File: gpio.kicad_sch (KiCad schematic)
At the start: 19 parts, among them J10 GPIO0, J13 GPIO1, J16 SCOOP1, J17 SCOOP2, J18 ACTUATOR, J19 DRILL, J20 SERVO5, J21 SERVO6, J22 SERVO7, J23 SERVO8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

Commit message: more cleanup and added notes for review
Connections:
- net Payload_S1: now also J10.1 (Pin_1), U8.4 (IO0_0); no longer J10.5 (Pin_5), U8.8 (IO0_4)
- net Payload_S2: now also J10.2 (Pin_2), U8.5 (IO0_1); no longer J10.6 (Pin_6), U8.9 (IO0_5)
- net Payload_S3: now also J10.3 (Pin_3), U8.6 (IO0_2); no longer J10.7 (Pin_7), U8.10 (IO0_6)
- net Payload_S4: now also J10.4 (Pin_4), U8.7 (IO0_3); no longer J10.8 (Pin_8), U8.11 (IO0_7)
- net GP21 renamed DIGITAL_GP21
- net GP22 renamed DIGITAL_GP22
- net NEW_GP14 renamed DIGITAL_GP14
- net NEW_GP15 renamed DIGITAL_GP15
- new net: J10.7 (Pin_7), U8.10 (IO0_6)
- new net: J10.8 (Pin_8), U8.11 (IO0_7)
- new net: J10.5 (Pin_5), U8.8 (IO0_4)
- new net: J10.6 (Pin_6), U8.9 (IO0_5)
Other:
- note added: "------ GET RID? -----"
- note added: "POSSIBILITIES!"
- note added: "WHAT DOES THE MANIPULATOR USE LABEL THE RELAYS FERRITES AND ESD?"

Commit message: DNP unused connectors for now
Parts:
- J10, J13, J20, J21, J22, J23: now not fitted
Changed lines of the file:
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@@
 		(in_bom yes)
 		(on_board yes)
-		(dnp no)
+		(dnp yes)
 		(fields_autoplaced yes)
 		(property "Reference" "J22"
@@
 		(in_bom yes)
 		(on_board yes)
-		(dnp no)
+		(dnp yes)
 		(fields_autoplaced yes)
 		(property "Reference" "J21"
@@
 		(in_bom yes)
 		(on_board yes)
-		(dnp no)
+		(dnp yes)
 		(fields_autoplaced yes)
 		(property "Reference" "J20"
@@
 		(in_bom yes)
 		(on_board yes)
-		(dnp no)
+		(dnp yes)
 		(fields_autoplaced yes)
 		(property "Reference" "J10"
@@
 		(in_bom yes)
 		(on_board yes)
-		(dnp no)
+		(dnp yes)
 		(fields_autoplaced yes)
 		(property "Reference" "J13"
@@
 		(in_bom yes)
 		(on_board yes)
-		(dnp no)
+		(dnp yes)
 		(fields_autoplaced yes)
 		(property "Reference" "J23"

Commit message: pcb review session notes
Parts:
- J9: value RELAYS -> GPIO
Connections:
- net DIGITAL_GP15 is gone; now on net DIGITAL_LIMIT_SW: J9.6 (Pin_6)
- net DIGITAL_GP14 renamed DIGITAL_LIMIT_SW
- net DIGITAL_GP21 renamed DIGITAL_RELAY1
- net DIGITAL_GP22 renamed DIGITAL_RELAY2
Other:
- note added: "LIMIT SWITCHES I2C to USB converter"
- moved on the sheet: J10, J13
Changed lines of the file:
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@@
 		)
 	)
+	(text "LIMIT SWITCHES\nI2C to USB converter"
+		(exclude_from_sim no)
+		(at 121.158 103.632 0)
+		(effects
+			(font
+				(size 2.54 2.54)
+				(thickness 0.508)
+				(bold yes)
+				(color 255 0 0 1)
+			)
+			(justify left top)
+		)
+	)
 	(text "3 and 4 go to the big\nconnector on Daedalus."
 		(exclude_from_sim no)
@@
 	(text "------ GET RID? -----\n"
 		(exclude_from_sim no)
-		(at 240.538 152.146 90)
+		(at 244.094 156.21 90)
 		(effects
 			(font
@@
 	(text "POSSIBILITIES!"
 		(exclude_from_sim no)
-		(at 46.482 150.622 0)
+		(at 33.274 150.114 0)
 		(effects
 			(font
@@
 	(wire
 		(pts
-			(xy 93.98 133.35) (xy 113.03 133.35)
+			(xy 93.98 133.35) (xy 114.3 133.35)
 		)
 		(stroke
@@
 	(wire
 		(pts
-			(xy 93.98 135.89) (xy 113.03 135.89)
+			(xy 93.98 135.89) (xy 114.3 135.89)
 		)
 		(stroke
@@
 	(wire
 		(pts
-			(xy 113.03 163.83) (xy 93.98 163.83)
+			(xy 114.3 163.83) (xy 93.98 163.83)
 		)
 		(stroke
@@
 	(wire
 		(pts
-			(xy 93.98 171.45) (xy 113.03 171.45)
+			(xy 93.98 171.45) (xy 114.3 171.45)
 		)
 		(stroke
@@
 	(wire
 		(pts
-			(xy 93.98 168.91) (xy 113.03 168.91)
+			(xy 93.98 168.91) (xy 114.3 168.91)
 		)
 		(stroke
@@
 	(wire
 		(pts
-			(xy 93.98 138.43) (xy 113.03 138.43)
+			(xy 93.98 138.43) (xy 114.3 138.43)
 		)
 		(stroke
@@
 	(wire
 		(pts
-			(xy 93.98 148.59) (xy 113.03 148.59)
+			(xy 93.98 148.59) (xy 114.3 148.59)
 		)
 		(stroke
@@
 	(wire
 		(pts
-			(xy 93.98 161.29) (xy 113.03 161.29)
+			(xy 93.98 161.29) (xy 114.3 161.29)
 		)
 		(stroke
@@
 	(wire
 		(pts
-			(xy 113.03 153.67) (xy 93.98 153.67)
+			(xy 114.3 153.67) (xy 93.98 153.67)
 		)
 		(stroke
@@
 	(wire
 		(pts
-			(xy 93.98 140.97) (xy 113.03 140.97)
+			(xy 93.98 140.97) (xy 114.3 140.97)
 		)
 		(stroke
@@
 	(wire
 		(pts
-			(xy 93.98 156.21) (xy 113.03 156.21)
+			(xy 93.98 156.21) (xy 114.3 156.21)
 		)
 		(stroke
@@
 	(wire
 		(pts
-			(xy 113.03 158.75) (xy 93.98 158.75)
+			(xy 114.3 158.75) (xy 93.98 158.75)
 		)
 		(stroke
@@
 	(wire
 		(pts
-			(xy 93.98 143.51) (xy 113.03 143.51)
+			(xy 93.98 143.51) (xy 114.3 143.51)
 		)
 		(stroke
@@
 	(wire
 		(pts
-			(xy 93.98 130.81) (xy 113.03 130.81)
+			(xy 93.98 130.81) (xy 114.3 130.81)
 		)
 		(stroke
@@
 	(wire
 		(pts
-			(xy 113.03 166.37) (xy 93.98 166.37)
+			(xy 114.3 166.37) (xy 93.98 166.37)
 		)
 		(stroke
@@
 	(wire
 		(pts
-			(xy 93.98 146.05) (xy 113.03 146.05)
+			(xy 93.98 146.05) (xy 114.3 146.05)
 		)
 		(stroke
@@
 		)
 	)
-	(global_label "DIGITAL_GP22"
+	(global_label "DIGITAL_RELAY2"
 		(shape input)
 		(at 115.57 57.15 180)
@@
 		)
 		(property "Intersheetrefs" "${INTERSHEET_REFS}"
-			(at 100.4785 57.15 0)
+			(at 98.6037 57.15 0)
 			(effects
 				(font
@@
 		)
 	)
-	(global_label "DIGITAL_GP15"
+	(global_label "DIGITAL_LIMIT_SW"
 		(shape input)
 		(at 115.57 62.23 180)
@@
 		)
 		(property "Intersheetrefs" "${INTERSHEET_REFS}"
-			(at 100.4785 62.23 0)
+			(at 97.1523 62.23 0)
 			(effects
 				(font
@@
 		)
 	)
-	(global_label "DIGITAL_GP14"
+	(global_label "DIGITAL_LIMIT_SW"
 		(shape input)
 		(at 115.57 59.69 180)
@@
 		)
 		(property "Intersheetrefs" "${INTERSHEET_REFS}"
-			(at 100.4785 59.69 0)
+			(at 97.1523 59.69 0)
 			(effects
 				(font
@@
 		)
 	)
-	(global_label "DIGITAL_GP21"
+	(global_label "DIGITAL_RELAY1"
 		(shape input)
 		(at 115.57 54.61 180)
@@
 		)
 		(property "Intersheetrefs" "${INTERSHEET_REFS}"
-			(at 100.4785 54.61 0)
+			(at 98.6037 54.61 0)
 			(effects
 				(font
@@
 	(symbol
 		(lib_id "Connector_Generic:Conn_01x08")
-		(at 118.11 138.43 0)
+		(at 119.38 138.43 0)
 		(unit 1)
 		(exclude_from_sim no)
@@
 		(fields_autoplaced yes)
 		(property "Reference" "J10"
-			(at 120.65 138.4299 0)
+			(at 121.92 138.4299 0)
 			(effects
 				(font
@@
 		)
 		(property "Value" "GPIO0"
-			(at 120.65 140.9699 0)
+			(at 121.92 140.9699 0)
 			(effects
 				(font
@@
 		)
 		(property "Footprint" "Connector_Molex:Molex_PicoBlade_53047-0810_1x08_P1.25mm_Vertical"
-			(at 118.11 138.43 0)
+			(at 119.38 138.43 0)
 			(effects
 				(font
@@
 		)
 		(property "Datasheet" "~"
-			(at 118.11 138.43 0)
+			(at 119.38 138.43 0)
 			(effects
 				(font
@@
 		)
 		(property "Description" "Generic connector, single row, 01x08, script generated (kicad-library-utils/schlib/autogen/connector/)"
-			(at 118.11 138.43 0)
+			(at 119.38 138.43 0)
 			(effects
 				(font
@@
 		)
 		(property "Manufacturer" ""
-			(at 118.11 138.43 0)
+			(at 119.38 138.43 0)
 			(effects
 				(font
@@
 		)
 		(property "Manufacturer Part Number" ""
-			(at 118.11 138.43 0)
+			(at 119.38 138.43 0)
 			(effects
 				(font
@@
 		)
 		(property "Vendor" ""
-			(at 118.11 138.43 0)
+			(at 119.38 138.43 0)
 			(effects
 				(font
@@
 		)
 		(property "Vendor Part Number" ""
-			(at 118.11 138.43 0)
+			(at 119.38 138.43 0)
 			(effects
 				(font
@@
 		)
 		(property "Comments" ""
-			(at 118.11 138.43 0)
+			(at 119.38 138.43 0)
 			(effects
 				(font
@@
 		)
 		(property "Notes" ""
-			(at 118.11 138.43 0)
+			(at 119.38 138.43 0)
 			(effects
 				(font
@@
 	(symbol
 		(lib_id "Connector_Generic:Conn_01x08")
-		(at 118.11 161.29 0)
+		(at 119.38 161.29 0)
 		(unit 1)
 		(exclude_from_sim no)
@@
 		(fields_autoplaced yes)
 		(property "Reference" "J13"
-			(at 120.65 161.2899 0)
+			(at 121.92 161.2899 0)
 			(effects
 				(font
@@
 		)
 		(property "Value" "GPIO1"
-			(at 120.65 163.8299 0)
+			(at 121.92 163.8299 0)
 			(effects
 				(font
@@
 		)
 		(property "Footprint" "Connector_Molex:Molex_PicoBlade_53047-0810_1x08_P1.25mm_Vertical"
-			(at 118.11 161.29 0)
+			(at 119.38 161.29 0)
 			(effects
 				(font
@@
 		)
 		(property "Datasheet" "~"
-			(at 118.11 161.29 0)
+			(at 119.38 161.29 0)
 			(effects
 				(font
@@
 		)
 		(property "Description" "Generic connector, single row, 01x08, script generated (kicad-library-utils/schlib/autogen/connector/)"
-			(at 118.11 161.29 0)
+			(at 119.38 161.29 0)
 			(effects
 				(font
@@
 		)
 		(property "Manufacturer" ""
-			(at 118.11 161.29 0)
+			(at 119.38 161.29 0)
 			(effects
 				(font
@@
 		)
 		(property "Manufacturer Part Number" ""
-			(at 118.11 161.29 0)
+			(at 119.38 161.29 0)
 			(effects
 				(font
@@
 		)
 		(property "Vendor" ""
-			(at 118.11 161.29 0)
+			(at 119.38 161.29 0)
 			(effects
 				(font
@@
 		)
 		(property "Vendor Part Number" ""
-			(at 118.11 161.29 0)
+			(at 119.38 161.29 0)
 			(effects
 				(font
@@
 		)
 		(property "Comments" ""
-			(at 118.11 161.29 0)
+			(at 119.38 161.29 0)
 			(effects
 				(font
@@
 		)
 		(property "Notes" ""
-			(at 118.11 161.29 0)
+			(at 119.38 161.29 0)
 			(effects
 				(font
@@
 			)
 		)
-		(property "Value" "RELAYS"
+		(property "Value" "GPIO"
 			(at 135.89 59.6899 0)
 			(effects

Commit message: major rework again after the meeting
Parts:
- removed J10: GPIO0, Connector_Molex:Molex_PicoBlade_53047-0810_1x08_P1.25mm_Vertical, symbol Connector_Generic:Conn_01x08
- removed J13: GPIO1, Connector_Molex:Molex_PicoBlade_53047-0810_1x08_P1.25mm_Vertical, symbol Connector_Generic:Conn_01x08
- removed J20: SERVO5, Connector_Molex:Molex_PicoBlade_53047-0310_1x03_P1.25mm_Vertical, symbol Connector_Generic:Conn_01x03
- removed J21: SERVO6, Connector_Molex:Molex_PicoBlade_53047-0310_1x03_P1.25mm_Vertical, symbol Connector_Generic:Conn_01x03
- removed J22: SERVO7, Connector_Molex:Molex_PicoBlade_53047-0310_1x03_P1.25mm_Vertical, symbol Connector_Generic:Conn_01x03
- removed J23: SERVO8, Connector_Molex:Molex_PicoBlade_53047-0310_1x03_P1.25mm_Vertical, symbol Connector_Generic:Conn_01x03
- removed R7: 10k, Resistor_SMD:R_0805_2012Metric_Pad1.20x1.40mm_HandSolder, symbol Device:R_US
- removed U15: 74HCT244, Package_SO:SO-20_12.8x7.5mm_P1.27mm, symbol 74xx:74HCT244
- removed U8: PCA9555PWR, Package_SO:TSSOP-24_4.4x7.8mm_P0.65mm, symbol Interface_Expansion:PCA9555DB
- added U1: SN74AHCT126DR, Package_SO:SOIC-14_3.9x8.7mm_P1.27mm, symbol symbols:SN74AHCT126DR
- J16: value SCOOP1 -> SCOOP
- J17: value SCOOP2 -> MANIPULATOR
- J18: value ACTUATOR -> SERVO3
- J19: value DRILL -> SERVO4
- J7: value POT3 -> MANIPULATOR
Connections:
- net VDC is gone; now on net +5V: C25.1, J16.1 (Pin_1), J17.1 (Pin_1), J18.1 (Pin_1), J19.1 (Pin_1)
- net +5V: now also U1.1 (1OE), U1.10 (3OE), U1.13 (4OE), U1.14 (VCC), U1.4 (2OE)
- net GND: now also U1.7 (GND)
- net SERVO1_OUT: now also U1.3 (1Y)
- net SERVO1_PICO: now also U1.2 (1A)
- net SERVO2_OUT: now also U1.6 (2Y)
- net SERVO2_PICO: now also U1.5 (2A)
- net SERVO3_OUT: now also U1.8 (3Y)
- net SERVO3_PICO: now also U1.9 (3A)
- net SERVO4_OUT: now also U1.11 (4Y)
- net SERVO4_PICO: now also U1.12 (4A)
- net ANALOG_POT3 renamed ANALOG_MANIPULATOR
- net DIGITAL_LIMIT_SW renamed DIGITAL_LIMIT_SW1
- net DIGITAL_LIMIT_SW1: no longer J9.6 (Pin_6)
- new net DIGITAL_LIMIT_SW2: J9.6 (Pin_6)
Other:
- note removed: "------ GET RID? -----"
- note removed: "Address: 0x20"
- note removed: "GPIO EXPANSION"
- note removed: "LIMIT SWITCHES I2C to USB converter"
- note removed: "NOTE: can use PCA9555 or TCA9555"
- note removed: "POSSIBILITIES!"
- note removed: "WHAT DOES THE MANIPULATOR USE LABEL THE RELAYS FERRITES AND ESD?"
- moved on the sheet: C23, C25, J16, J17, J18, J19, J5, J6, J7, J9

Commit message: major finishing touches:     - major rework for v5.1     - silkscreen and stuff     - impednace for USB and CAN lines     - schematic comments     - symbol, footprint, and model library updates
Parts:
- added C10: 1000uF, Capacitor_THT:CP_Radial_D10.0mm_P5.00mm, symbol Device:C_Polarized_US
- added J10: QWIIC3, Connector_JST:JST_GH_BM04B-GHS-TBT_1x04-1MP_P1.25mm_Vertical, symbol Connector_Generic:Conn_01x04
- added J11: QWIIC2, Connector_JST:JST_GH_BM04B-GHS-TBT_1x04-1MP_P1.25mm_Vertical, symbol Connector_Generic:Conn_01x04
- added J13: QWIIC1, Connector_JST:JST_GH_BM04B-GHS-TBT_1x04-1MP_P1.25mm_Vertical, symbol Connector_Generic:Conn_01x04
- added J20: EXP1, Connector_PinSocket_2.54mm:PinSocket_1x06_P2.54mm_Vertical, symbol Connector_Generic:Conn_01x06
- added J21: EXP2, Connector_PinSocket_2.54mm:PinSocket_1x06_P2.54mm_Vertical, symbol Connector_Generic:Conn_01x06
- added J22: EXP3, Connector_PinSocket_2.54mm:PinSocket_1x06_P2.54mm_Vertical, symbol Connector_Generic:Conn_01x06
- added J23: EXP4, Connector_PinSocket_2.54mm:PinSocket_1x06_P2.54mm_Vertical, symbol Connector_Generic:Conn_01x06
- added J8: QWIIC4, Connector_JST:JST_GH_BM04B-GHS-TBT_1x04-1MP_P1.25mm_Vertical, symbol Connector_Generic:Conn_01x04
- added R11, R12, R13, R14, R15, R16: 10k, Resistor_SMD:R_0603_1608Metric_Pad0.98x0.95mm_HandSolder, symbol Device:R_US
- added SW1: QUIIC, Button_Switch_THT:SW_E-Switch_EG1271_SPDT, symbol Switch:SW_SPDT
- added SW2: EXP, Button_Switch_THT:SW_E-Switch_EG1271_SPDT, symbol Switch:SW_SPDT
- C23: value 0.1 uF -> 0.1uF; Manufacturer (none) -> KEMET; Manufacturer Part Number (none) -> C1206C104J5RACTU; Vendor (none) -> Digikey; Vendor Part Number (none) -> 399-C1206C104J5RACTUCT-ND
- C25: value 100 uF -> 1000uF; Manufacturer (none) -> Nichicon; Manufacturer Part Number (none) -> UVR1E102MPD; Vendor (none) -> Digikey; Vendor Part Number (none) -> 493-1065-ND
- J16: renamed from J19; Manufacturer (none) -> Molex; Manufacturer Part Number (none) -> 0530470310; Vendor (none) -> Digikey; Vendor Part Number (none) -> WM1732-ND
- J17: renamed from J18; Manufacturer (none) -> Molex; Manufacturer Part Number (none) -> 0530470310; Vendor (none) -> Digikey; Vendor Part Number (none) -> WM1732-ND
- J18: renamed from J17; Manufacturer (none) -> Molex; Manufacturer Part Number (none) -> 0530470310; Vendor (none) -> Digikey; Vendor Part Number (none) -> WM1732-ND
- J19: renamed from J16; Manufacturer (none) -> Molex; Manufacturer Part Number (none) -> 0530470310; Vendor (none) -> Digikey; Vendor Part Number (none) -> WM1732-ND
- J5: value MOIST -> MST; Manufacturer (none) -> Molex; Manufacturer Part Number (none) -> 0530470310; Vendor (none) -> Digikey; Vendor Part Number (none) -> WM1732-ND
- J6: value TEMP -> TMP; Manufacturer (none) -> Molex; Manufacturer Part Number (none) -> 0530470310; Vendor (none) -> Digikey; Vendor Part Number (none) -> WM1732-ND
- J7: value MANIPULATOR -> MPR; Manufacturer (none) -> Molex; Manufacturer Part Number (none) -> 0530470310; Vendor (none) -> Digikey; Vendor Part Number (none) -> WM1732-ND
- J9: value GPIO -> DIGITAL; Manufacturer (none) -> Molex; Manufacturer Part Number (none) -> 0530470810; Vendor (none) -> Digikey; Vendor Part Number (none) -> WM1737-ND
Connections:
- net +5V: now also J9.1 (Pin_1), SW1.3 (C), SW2.3 (C); no longer J9.2 (Pin_2)
- net DIGITAL_LIMIT_SW1: now also R11.1
- net DIGITAL_LIMIT_SW2: now also R12.1
- net GND: now also C10.2, J10.1 (Pin_1), J11.1 (Pin_1), J13.1 (Pin_1), J20.1 (Pin_1), J21.1 (Pin_1), J22.1 (Pin_1), J23.1 (Pin_1), J8.1 (Pin_1), R15.1, R16.1
- net +3.3V renamed +3V3
- net +3V3: now also J9.2 (Pin_2), R11.2, R12.2, SW1.1 (A), SW2.1 (A); no longer J9.1 (Pin_1)
- new net +EXP: C10.1, J20.2 (Pin_2), J21.2 (Pin_2), J22.2 (Pin_2), J23.2 (Pin_2), R13.2, R14.2, SW2.2 (B)
- new net +QUIIC: J10.2 (Pin_2), J11.2 (Pin_2), J13.2 (Pin_2), J8.2 (Pin_2), SW1.2 (B)
- new net DIGITAL_EXP1: J20.5 (Pin_5), J21.5 (Pin_5), J22.5 (Pin_5), J23.5 (Pin_5), R13.1, R16.2
- new net DIGITAL_EXP2: J20.6 (Pin_6), J21.6 (Pin_6), J22.6 (Pin_6), J23.6 (Pin_6), R14.1, R15.2
- new net I2C0_SCL: J10.4 (Pin_4), J11.4 (Pin_4), J13.4 (Pin_4), J20.4 (Pin_4), J21.4 (Pin_4), J22.4 (Pin_4), J23.4 (Pin_4), J8.4 (Pin_4)
- new net I2C0_SDA: J10.3 (Pin_3), J11.3 (Pin_3), J13.3 (Pin_3), J20.3 (Pin_3), J21.3 (Pin_3), J22.3 (Pin_3), J23.3 (Pin_3), J8.3 (Pin_3)
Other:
- note added: "CUSTOM EXPANSION MODULES"
- note added: "Optional room for custom modules developed in house for flexibility and future-proofing."
- note added: "STEMMA QT / QWIIC MODULES"
- note added: "Standardized 4-pin I2C connectors that allow easy, solder-free chaining of off-the-shelf sensors and peripherals."
- company: WVU Unviersity Rover Challenge -> WVU Unviersity Rover Challenge (URC)
- moved on the sheet: C23, C25, J16, J17, J18, J19, J5, J6, J7, J9, U1

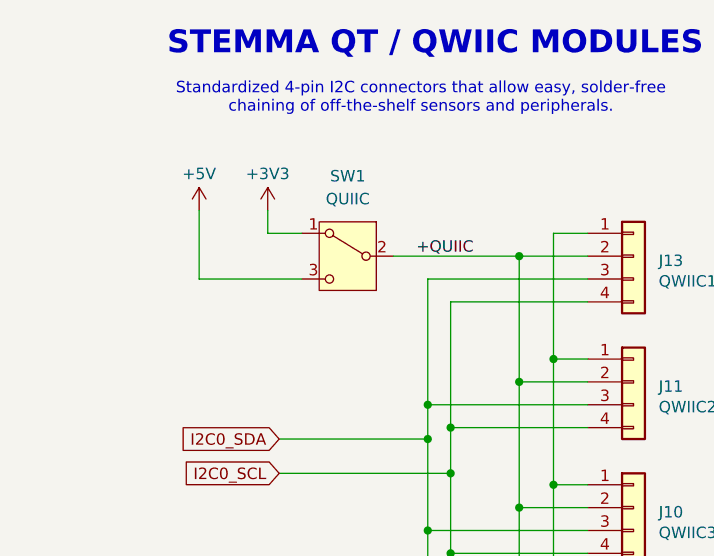
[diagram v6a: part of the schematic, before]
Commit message: swapped UART to USB from FTDI (out of stock) to MCP2200
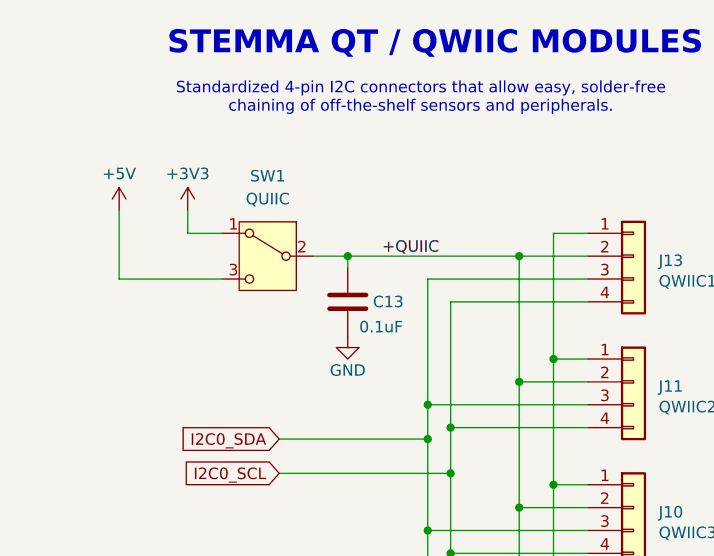
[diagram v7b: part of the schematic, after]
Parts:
- added C13: 0.1uF, Capacitor_SMD:C_1206_3216Metric_Pad1.33x1.80mm_HandSolder, symbol Device:C
- J10, J11, J13, J8: Manufacturer Part Number 455-1566-1-ND -> SM04B-GHS-TB; Vendor Part Number SM04B-GHS-TB -> 455-1566-1-ND
- J20, J21, J22, J23: Manufacturer Part Number SAM10025-ND -> SSW-106-01-F-S
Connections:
- net +QUIIC: now also C13.2
- net GND: now also C13.1
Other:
- moved on the sheet: SW1
